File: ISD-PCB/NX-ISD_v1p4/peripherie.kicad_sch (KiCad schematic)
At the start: 34 parts, among them J2 1-2328702-0, Q3 AO3400A, Q4 AO3400A, U14 ZDSD02GLGEAG, U16 TM-2025A

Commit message: feat(pcb): v1.4 schematic and layout updates for 4-bit SDMMC, direct display SPI, and button pullups
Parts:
- removed R20, R21, R22: 51.1k, Resistor_SMD:R_0402_1005Metric, symbol Device:R
- removed R30: 10k, Resistor_SMD:R_0402_1005Metric, symbol Device:R
- removed U14: ZDSD02GLGEAG, NX-AW-footprints:LGA-8_L8.0-W6.0-P1.27-TL_ZDSD02GLGEAG, symbol ZDSD02GLGEAG:ZDSD02GLGEAG
- added C28: 100n, Capacitor_SMD:C_0402_1005Metric, symbol Device:C
- added J4: Micro_SD_Card, Connector_Card:microSD_HC_Wuerth_693072010801, symbol Connector:Micro_SD_Card
- C27: value 100n -> 10u; footprint Capacitor_SMD:C_0402_1005Metric -> Capacitor_SMD:C_0603_1608Metric
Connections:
- net +3V3: now also C28.1, J4.4 (VDD)
- net GND: now also C28.2, J4.6 (VSS), J4.SH (SHIELD)
- net CS_TFT renamed TFT_CS
- no-connect marks 5 -> 3
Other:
- note added: "[0603]"

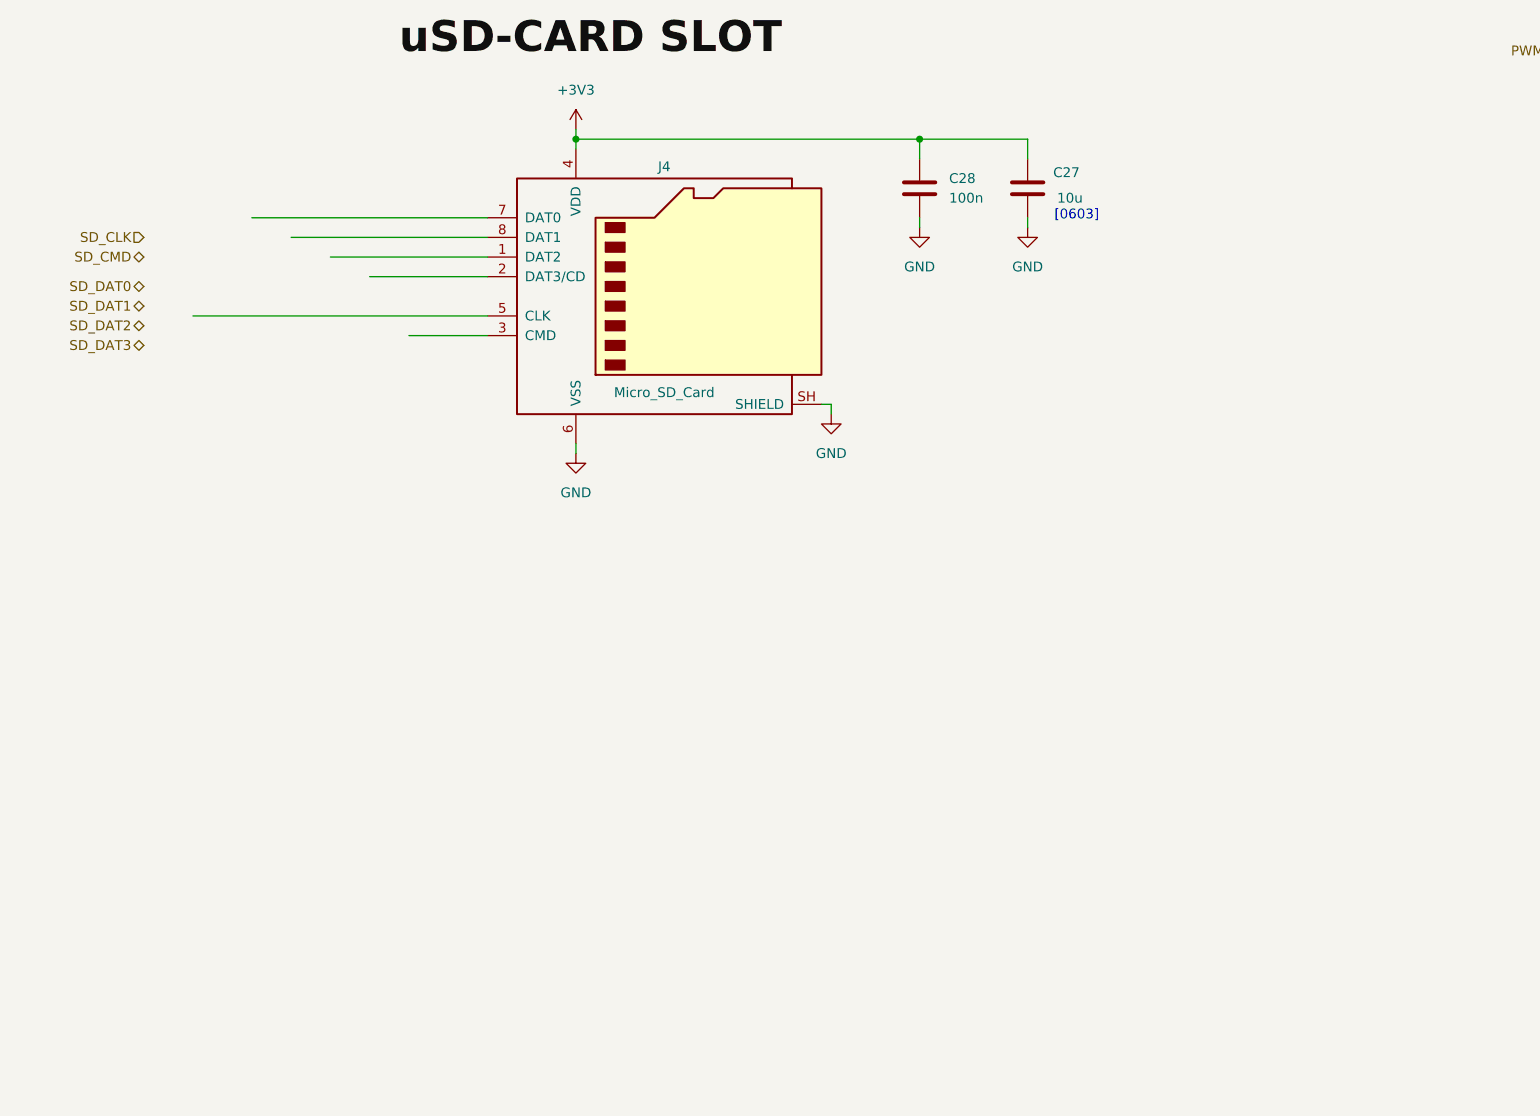
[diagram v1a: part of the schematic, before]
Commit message: hw(v1.4): relocate MicroSD to right edge and re-route BNO085 cluster; update READMEs
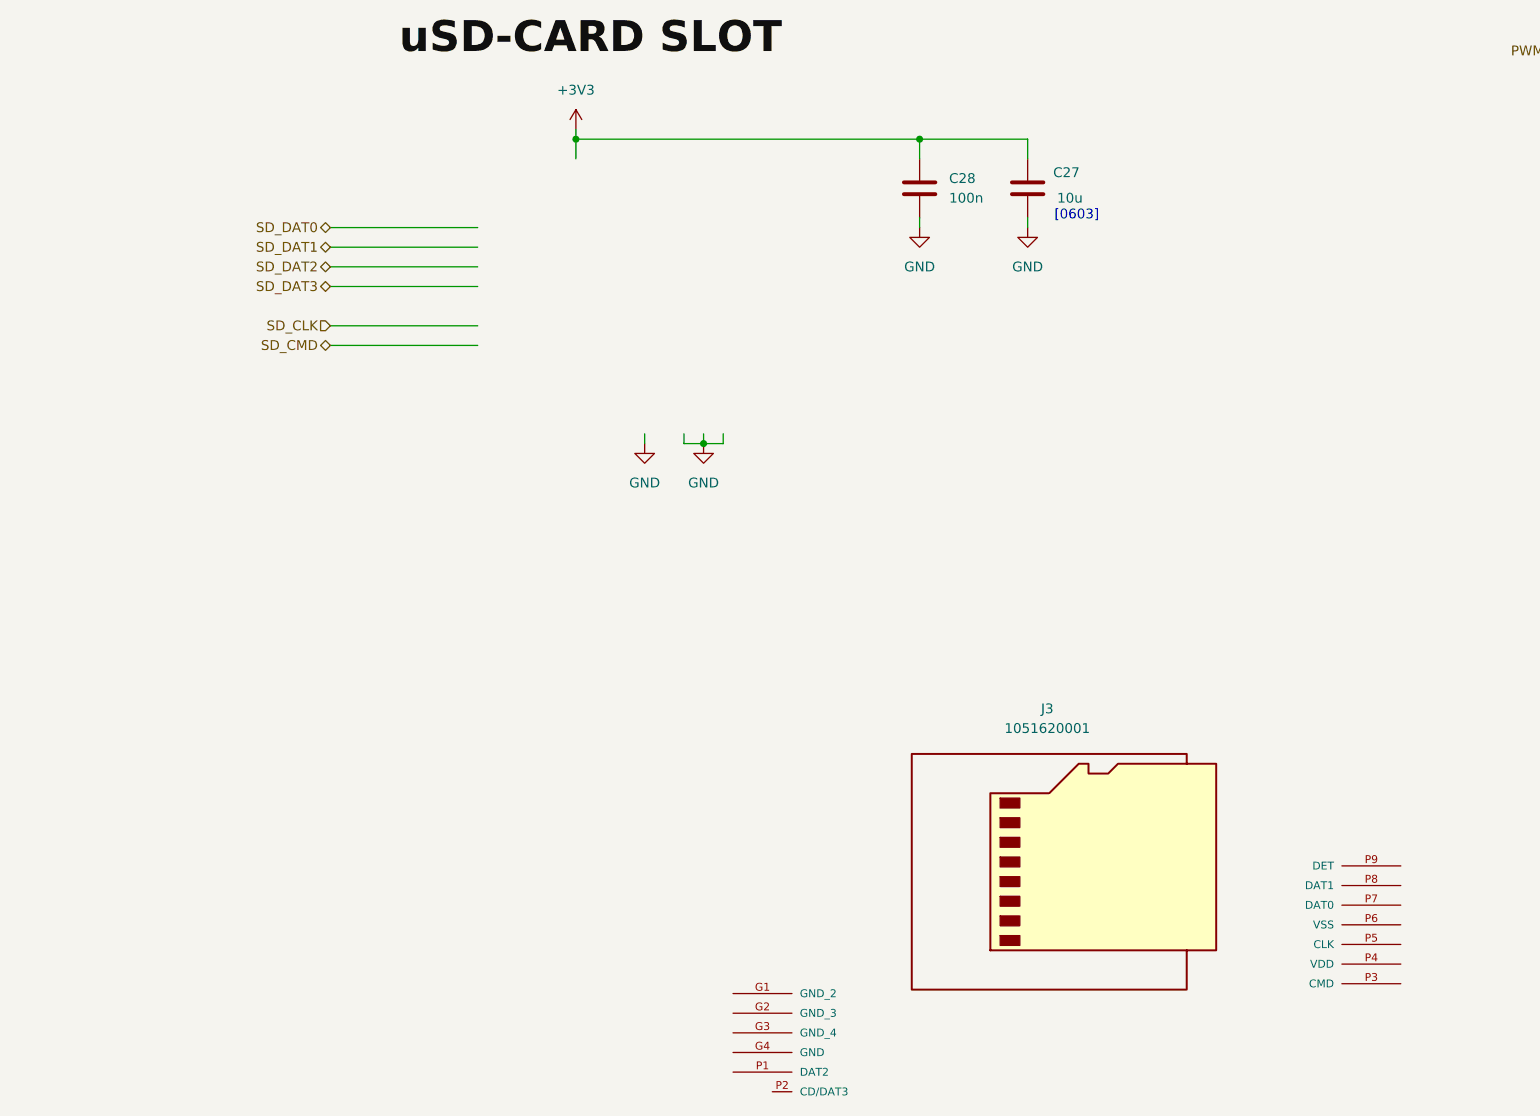
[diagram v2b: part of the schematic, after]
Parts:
- removed J4: Micro_SD_Card, Connector_Card:microSD_HC_Wuerth_693072010801, symbol Connector:Micro_SD_Card
- added J3: 1051620001, NX-AW-footprints:105162-0001_MOL, symbol 1051620001:1051620001

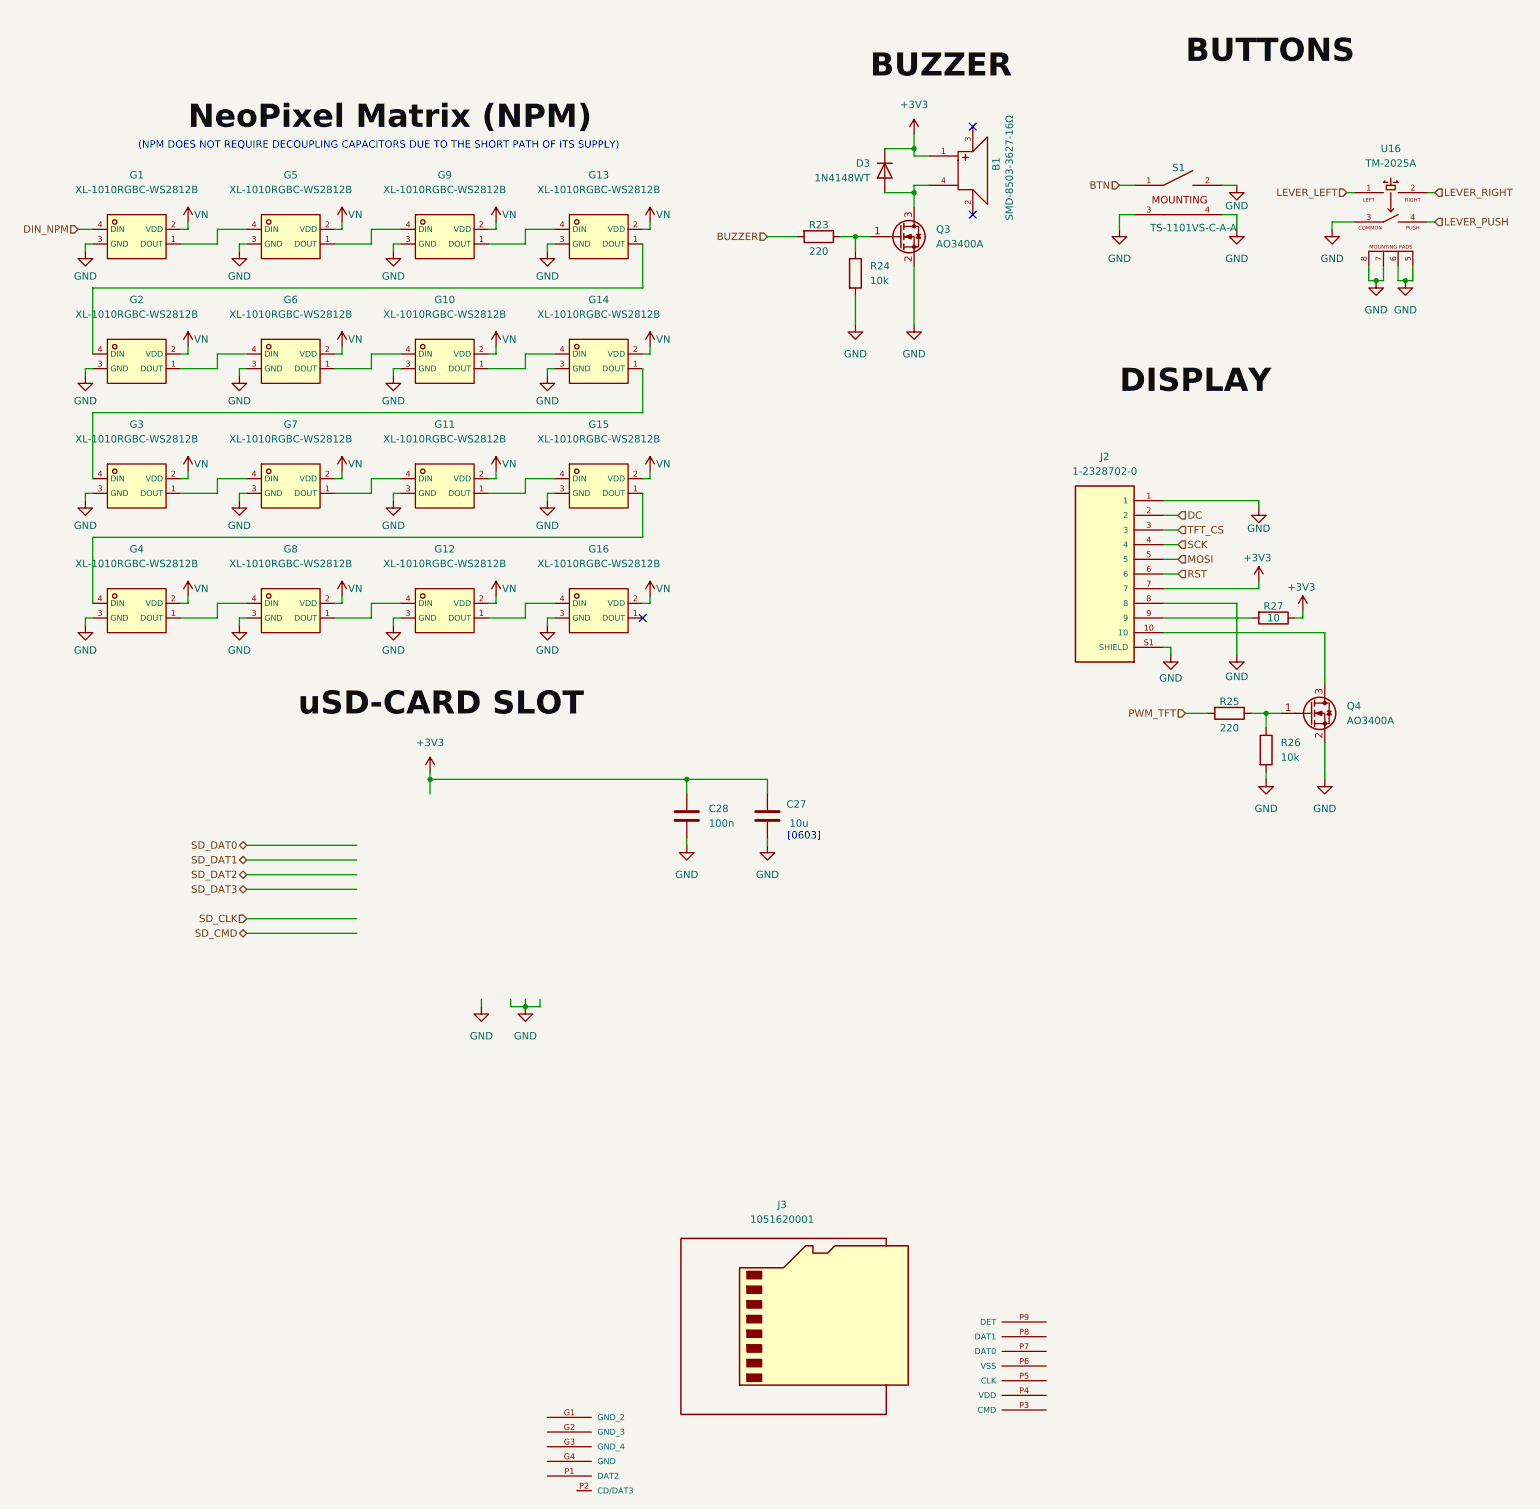
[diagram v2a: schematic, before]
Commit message: hw(v1.4): progress on TODO - 4-bit MicroSD, direct display bus, BNO085 & EP vias (DRC 0 errors)
- Implemented 4-bit SDMMC MicroSD slot (Molex 105162-0001) on right edge with outward insertion
- Routed direct 3.3V display SPI bus (TE 1-2328702-0) with C29 100nF decoupling
- Centered BNO085 9-DOF IMU cluster with local ground star and 32.768kHz crystal
- Rerouted NeoPixel PWR_NPM high-side power gate signal
- Updated thermal EP pad via sizes on BQ25170 and MAX17048 for standard JLCPCB fabrication
- Achieved 0 DRC errors, 0 unconnected nets, and 100% schematic parity
- Updated HW-TODO and SW-TODO for v1.3/v1.4 pinout target abstraction
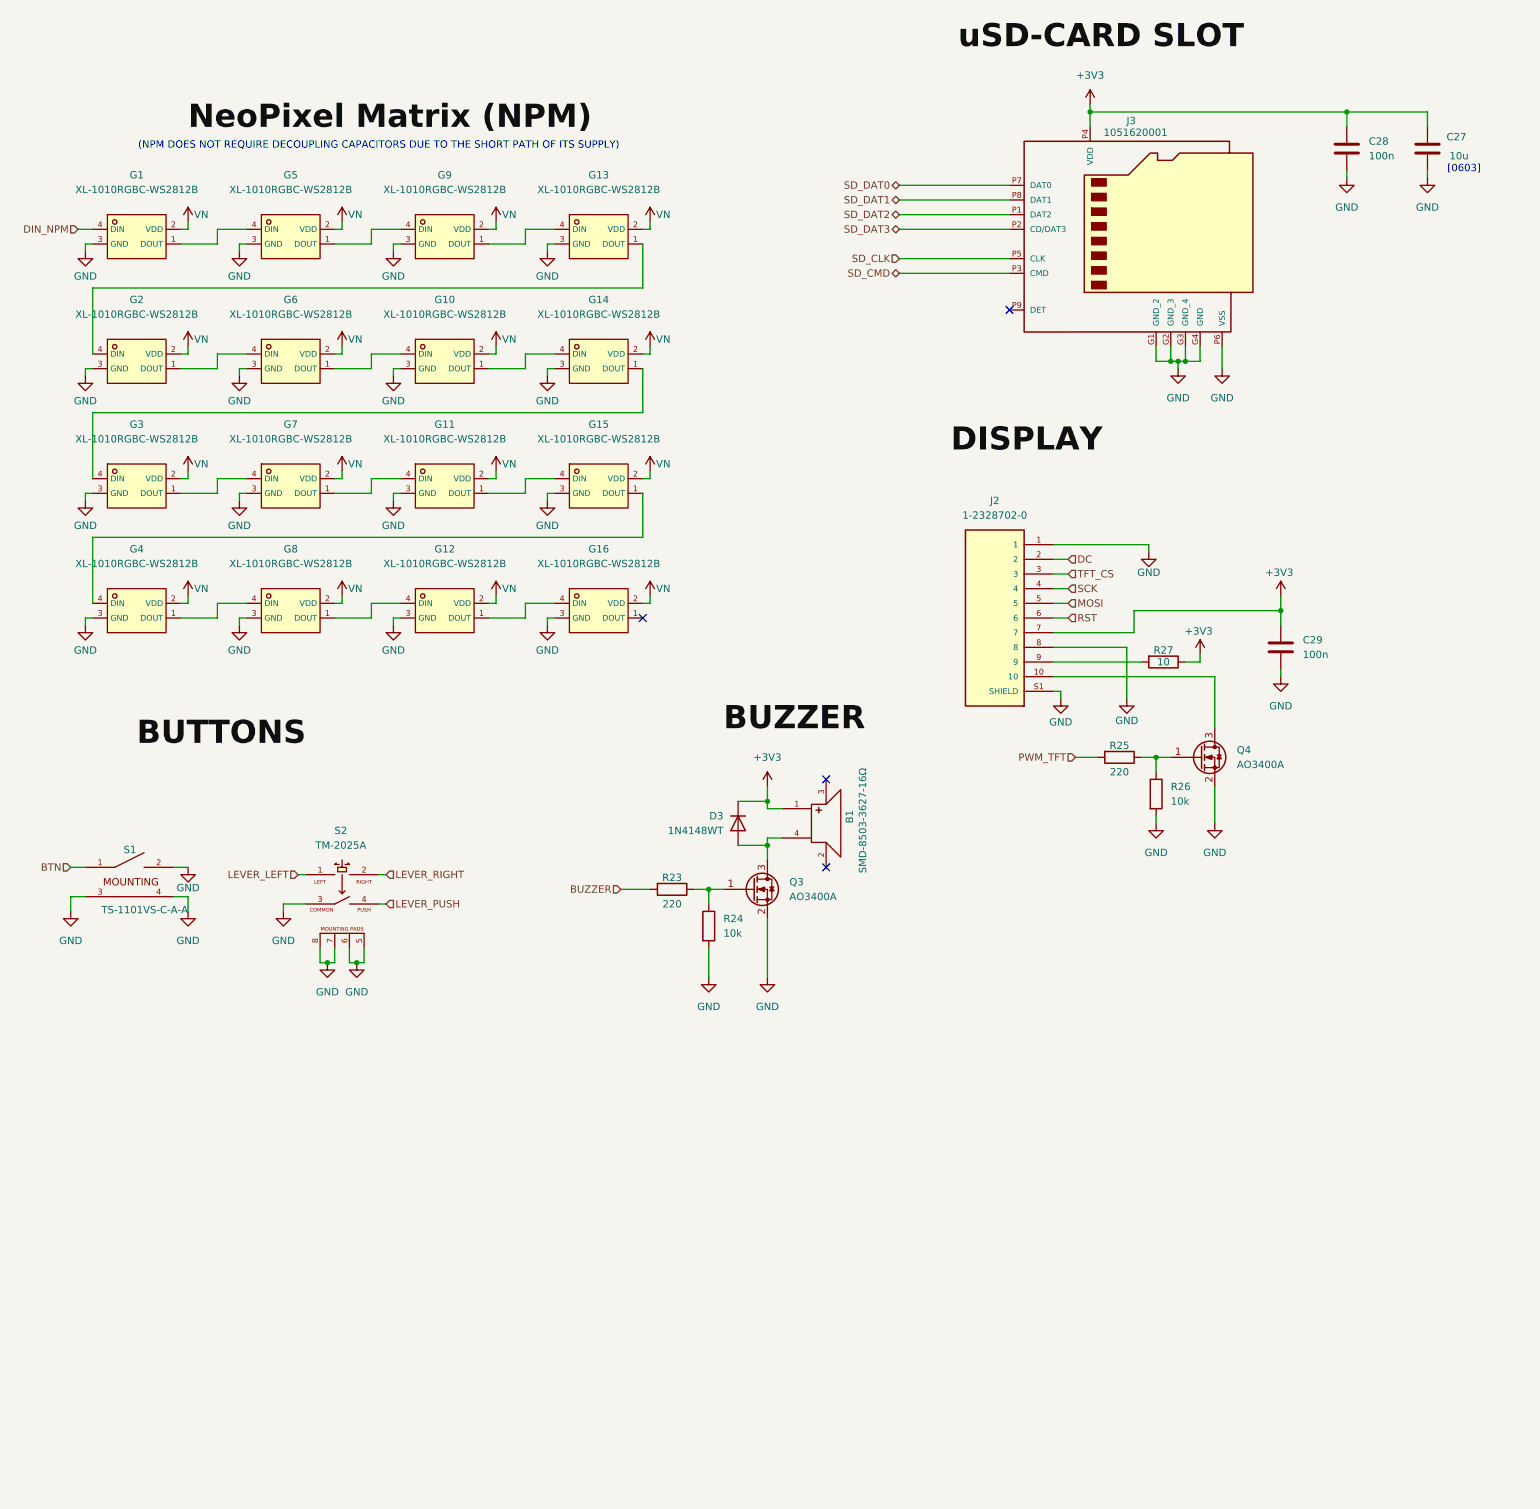
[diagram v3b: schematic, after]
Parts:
- added C29: 100n, Capacitor_SMD:C_0402_1005Metric, symbol Device:C
- renumbered U16 to S2
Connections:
- net +3V3: now also J3.P4 (VDD), C29.1
- net GND: now also J3.G1 (GND_2), J3.G2 (GND_3), J3.G3 (GND_4), J3.G4 (GND), J3.P6 (VSS), C29.2
- net SD_CLK: now also J3.P5 (CLK)
- net SD_CMD: now also J3.P3 (CMD)
- net SD_DAT0: now also J3.P7 (DAT0)
- net SD_DAT1: now also J3.P8 (DAT1)
- net SD_DAT2: now also J3.P1 (DAT2)
- net SD_DAT3: now also J3.P2 (CD/DAT3)
- no-connect marks 3 -> 4
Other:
- moved on the sheet: B1, C27, C28, D3, J2, J3, Q3, Q4, R23, R24, R25, R26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

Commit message: hw(v1.4): bq25170 thermal optimization, usb-c plating, battery pad stitching, and npm decoupling
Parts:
- added C34, C36: 100n, Capacitor_SMD:C_0402_1005Metric, symbol Device:C
- added C35, C37: 4.7u, Capacitor_SMD:C_0603_1608Metric, symbol Device:C
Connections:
- net GND: now also C34.2, C35.2, C36.2, C37.2
- net VN: now also C34.1, C35.1, C36.1, C37.1
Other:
- note added: "(FOR STABALIZING THE NPM RECEIVES TWO BULK CAPACITOR PAIRS ON LEFT AND RIGHT)"
- note removed: "(NPM DOES NOT REQUIRE DECOUPLING CAPACITORS DUE TO THE SHORT PATH OF ITS SUPPLY)"
- title: (none) -> NX-ISD Version 1 Rev. 4

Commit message: hw(v1p4): add RTC backup supercap C27, tactile buttons, USBLC6 footprint adjustments, and cyberpunk silkscreens
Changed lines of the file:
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@@
 		(fields_autoplaced yes)
 		(property "Reference" "J3"
-			(at 207.772 34.544 0)
+			(at 229.87 53.3399 0)
 			(show_name no)
 			(do_not_autoplace no)
@@
 					(size 1.27 1.27)
 				)
+				(justify left)
 			)
 		)
 		(property "Value" "1051620001"
-			(at 208.534 36.576 0)
+			(at 229.87 55.8799 0)
 			(show_name no)
 			(do_not_autoplace no)
@@
 					(size 1.27 1.27)
 				)
+				(justify left)
 			)
 		)
